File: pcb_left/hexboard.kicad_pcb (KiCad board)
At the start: 2 copper layers, 121.4 x 97.6 mm, 39 parts, among them J1 Conn_01x02_Pin, SW1 SW_Push_45deg, SW10 SW_Push_45deg, SW11 SW_Push_45deg, SW12 SW_Push_45deg, SW13 SW_Push_45deg, SW14 SW_Push_45deg, SW15 SW_Push_45deg, SW16 SW_Push_45deg, SW17 SW_Push_45deg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

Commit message: Committing any uncommitted changes
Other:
- board size 121.4 x 97.6 mm -> 209 x 97.6 mm
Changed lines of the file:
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@@
-	)
-	(gr_line
-		(start 165.590197 103.793303)
-		(end 146.590197 103.793303)
-		(stroke
-			(width 0.05)
-			(type default)
-		)
-		(layer "Edge.Cuts")
-	)
-	(gr_line
-		(start 146.090197 103.293303)
-		(end 146.090197 71.793303)
-		(stroke
-			(width 0.05)
-			(type default)
-		)
-		(layer "Edge.Cuts")
 	)
 	(gr_line
@@
 		(start 67.503125 38.1625)
 		(end 84.171875 38.1625)
+		(stroke
+			(width 0.05)
+			(type default)
+		)
+		(layer "Edge.Cuts")
+	)
+	(gr_arc
+		(start 256.2625 112.925)
+		(mid 255.969607 113.632107)
+		(end 255.2625 113.925)
 		(stroke
 			(width 0.05)
@@
 		(layer "Edge.Cuts")
 	)
-	(gr_arc
-		(start 165.590197 71.293303)
-		(mid 165.943718 71.439767)
-		(end 166.090197 71.793303)
-		(stroke
-			(width 0.05)
-			(type default)
-		)
-		(layer "Edge.Cuts")
-	)
 	(gr_line
 		(start 105.603125 38.1625)
@@
 		(layer "Edge.Cuts")
 	)
-	(gr_line
-		(start 166.090197 71.793303)
-		(end 166.090197 103.293303)
+	(gr_arc
+		(start 235.2625 113.925)
+		(mid 234.555393 113.632107)
+		(end 234.2625 112.925)
 		(stroke
 			(width 0.05)
@@
 		(layer "Edge.Cuts")
 	)
-	(gr_arc
-		(start 146.090197 71.793303)
-		(mid 146.236641 71.439732)
-		(end 146.590197 71.293303)
-		(stroke
-			(width 0.05)
-			(type default)
-		)
-		(layer "Edge.Cuts")
-	)
 	(gr_line
 		(start 86.553125 35.78125)
@@
 		(layer "Edge.Cuts")
 	)
-	(gr_arc
-		(start 146.590197 103.793303)
-		(mid 146.236676 103.646839)
-		(end 146.090197 103.293303)
+	(gr_line
+		(start 255.2625 81.925)
+		(end 235.2625 81.925)
 		(stroke
 			(width 0.05)
@@
 		(layer "Edge.Cuts")
 	)
-	(gr_arc
-		(start 166.090197 103.293303)
-		(mid 165.943753 103.646874)
-		(end 165.590197 103.793303)
+	(gr_line
+		(start 256.2625 112.925)
+		(end 256.2625 82.925)
 		(stroke
 			(width 0.05)
@@
 		(layer "Edge.Cuts")
 	)
+	(gr_line
+		(start 235.2625 113.925)
+		(end 255.2625 113.925)
+		(stroke
+			(width 0.05)
+			(type default)
+		)
+		(layer "Edge.Cuts")
+	)
 	(gr_arc
 		(start 66.3125 39.353125)
@@
 	)
 	(gr_arc
+		(start 255.2625 81.925)
+		(mid 255.969607 82.217893)
+		(end 256.2625 82.925)
+		(stroke
+			(width 0.05)
+			(type default)
+		)
+		(layer "Edge.Cuts")
+	)
+	(gr_arc
 		(start 85.3625 36.971875)
 		(mid 85.711233 36.129983)
@@
 		(layer "Edge.Cuts")
 	)
+	(gr_arc
+		(start 234.2625 82.925)
+		(mid 234.555393 82.217893)
+		(end 235.2625 81.925)
+		(stroke
+			(width 0.05)
+			(type default)
+		)
+		(layer "Edge.Cuts")
+	)
 	(gr_line
 		(start 93.696875 122.696875)
 		(end 85.3625 100.075)
-		(stroke
-			(width 0.05)
-			(type default)
-		)
-		(layer "Edge.Cuts")
-	)
-	(gr_line
-		(start 146.590197 71.293303)
-		(end 165.590197 71.293303)
 		(stroke
 			(width 0.05)
@@
 		(start 152.0375 133.4125)
 		(end 132.9875 126.26875)
+		(stroke
+			(width 0.05)
+			(type default)
+		)
+		(layer "Edge.Cuts")
+	)
+	(gr_line
+		(start 234.2625 82.925)
+		(end 234.2625 112.925)
 		(stroke
 			(width 0.05)
@@
 		)
 	)
-	(group ""
-		(members "038aaf56-ff1c-4074-8000-df0718c7a4ec" "0e31a366-141b-4baf-99b6-0dca1101d026"
-			"40619495-6268-4496-b2b6-aa191c0de21f" "506f3372-851e-4a31-bfa3-b7644925351c"
-			"635464b2-ef81-4934-a91e-93d34530852f" "79b33994-54df-4e0b-a44d-c605a84cba06"
-			"7f5ebb2b-8fa1-485b-92b2-fea6a831ab9d" "b6ac122d-b97c-4c0c-a1d2-f78f0358de96"
-		)
-	)

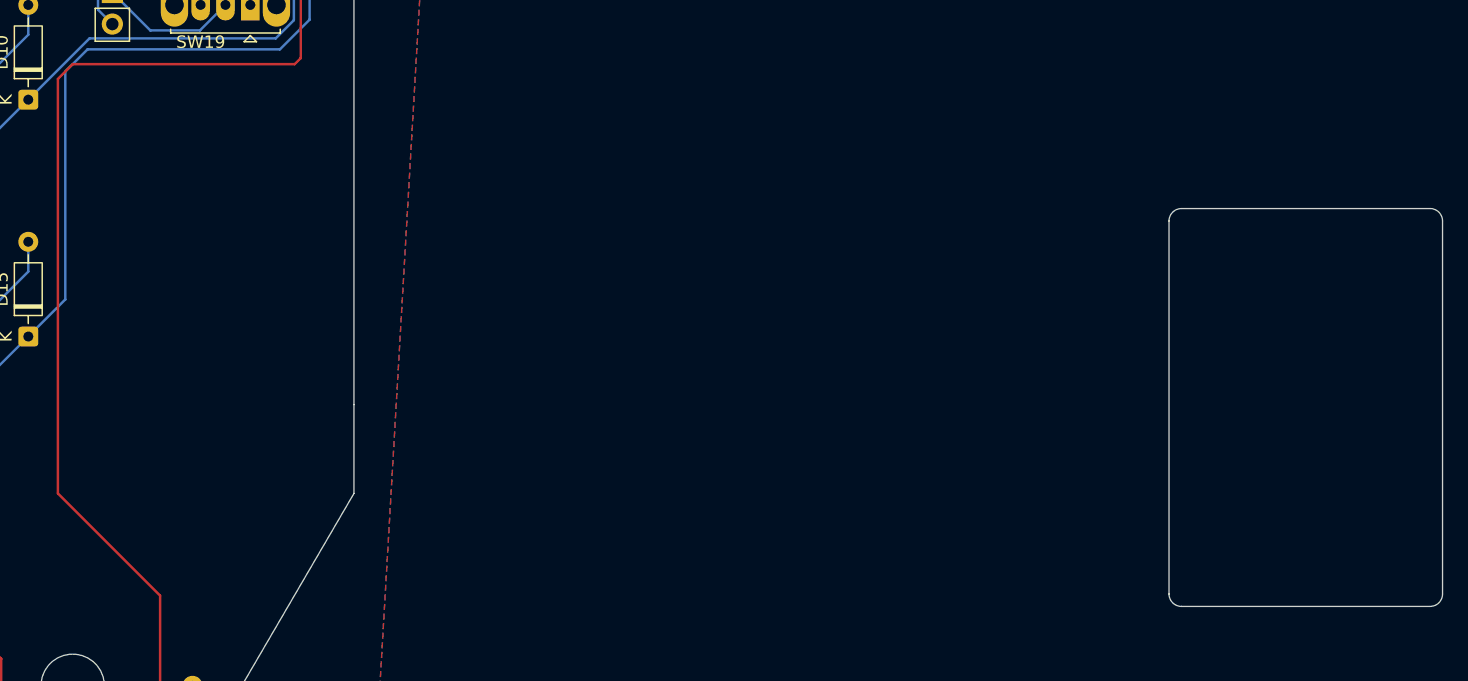
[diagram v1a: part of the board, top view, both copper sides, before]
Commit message: added design to case, colorized 3mf files
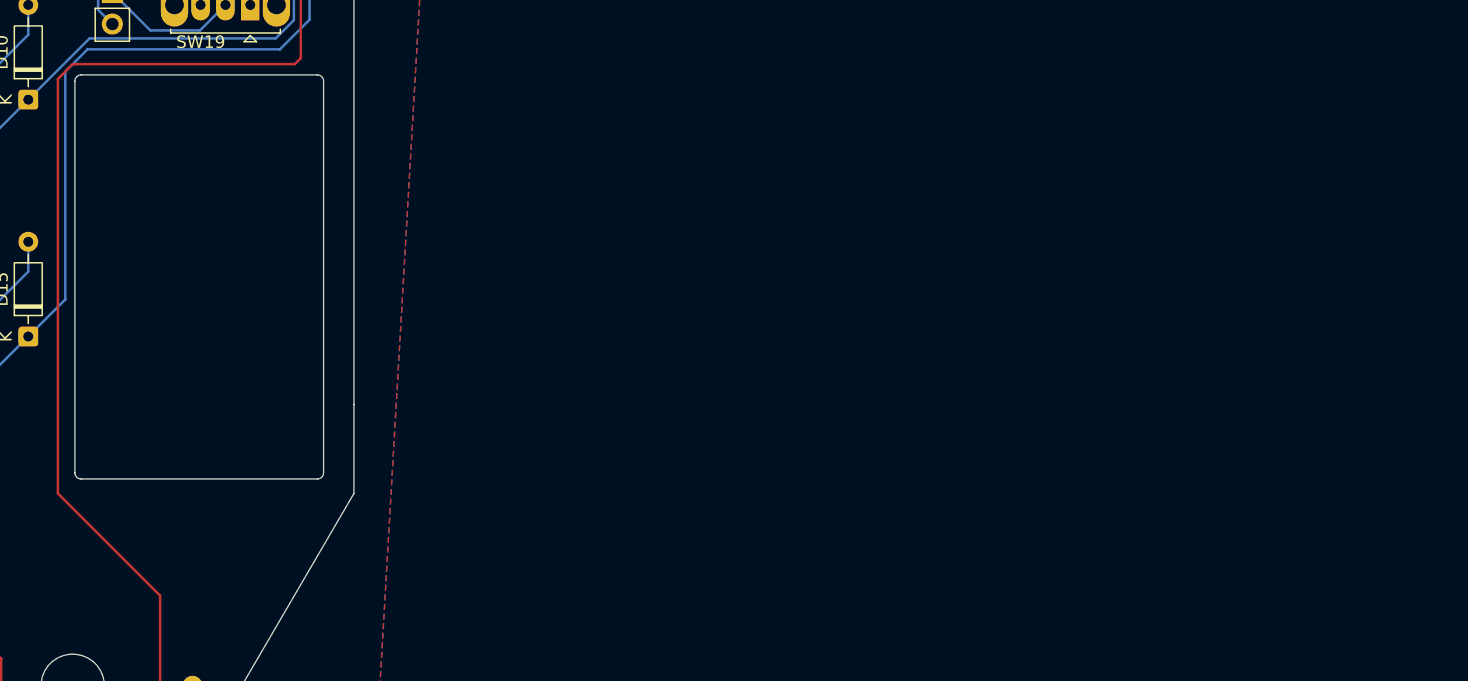
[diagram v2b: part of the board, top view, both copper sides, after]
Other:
- board size 209 x 97.6 mm -> 121.4 x 97.6 mm
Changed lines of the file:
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@@
 		(embedded_fonts no)
+	)
+	(gr_arc
+		(start 166.2625 103.175)
+		(mid 166.116023 103.528523)
+		(end 165.7625 103.675)
+		(stroke
+			(width 0.05)
+			(type default)
+		)
+		(layer "Edge.Cuts")
+	)
+	(gr_line
+		(start 146.7625 103.675)
+		(end 165.7625 103.675)
+		(stroke
+			(width 0.05)
+			(type default)
+		)
+		(layer "Edge.Cuts")
 	)
 	(gr_line
@@
 		(start 67.503125 38.1625)
 		(end 84.171875 38.1625)
-		(stroke
-			(width 0.05)
-			(type default)
-		)
-		(layer "Edge.Cuts")
-	)
-	(gr_arc
-		(start 256.2625 112.925)
-		(mid 255.969607 113.632107)
-		(end 255.2625 113.925)
 		(stroke
 			(width 0.05)
@@
 		(layer "Edge.Cuts")
 	)
+	(gr_line
+		(start 166.2625 103.175)
+		(end 166.2625 71.675)
+		(stroke
+			(width 0.05)
+			(type default)
+		)
+		(layer "Edge.Cuts")
+	)
 	(gr_arc
 		(start 105.603125 38.1625)
@@
 		(layer "Edge.Cuts")
 	)
-	(gr_arc
-		(start 235.2625 113.925)
-		(mid 234.555393 113.632107)
-		(end 234.2625 112.925)
+	(gr_line
+		(start 165.7625 71.175)
+		(end 146.7625 71.175)
 		(stroke
 			(width 0.05)
@@
 	)
 	(gr_line
-		(start 255.2625 81.925)
-		(end 235.2625 81.925)
-		(stroke
-			(width 0.05)
-			(type default)
-		)
-		(layer "Edge.Cuts")
-	)
-	(gr_line
 		(start 66.3125 41.734375)
 		(end 66.3125 39.353125)
@@
 		(layer "Edge.Cuts")
 	)
-	(gr_line
-		(start 256.2625 112.925)
-		(end 256.2625 82.925)
+	(gr_arc
+		(start 165.7625 71.175)
+		(mid 166.11605 71.321448)
+		(end 166.2625 71.675)
 		(stroke
 			(width 0.05)
@@
 		(layer "Edge.Cuts")
 	)
-	(gr_line
-		(start 235.2625 113.925)
-		(end 255.2625 113.925)
+	(gr_arc
+		(start 146.2625 71.675)
+		(mid 146.408975 71.321475)
+		(end 146.7625 71.175)
 		(stroke
 			(width 0.05)
@@
 	)
 	(gr_arc
-		(start 255.2625 81.925)
-		(mid 255.969607 82.217893)
-		(end 256.2625 82.925)
-		(stroke
-			(width 0.05)
-			(type default)
-		)
-		(layer "Edge.Cuts")
-	)
-	(gr_arc
 		(start 85.3625 36.971875)
 		(mid 85.711233 36.129983)
@@
 		(layer "Edge.Cuts")
 	)
-	(gr_arc
-		(start 234.2625 82.925)
-		(mid 234.555393 82.217893)
-		(end 235.2625 81.925)
-		(stroke
-			(width 0.05)
-			(type default)
-		)
-		(layer "Edge.Cuts")
-	)
 	(gr_line
 		(start 93.696875 122.696875)
 		(end 85.3625 100.075)
+		(stroke
+			(width 0.05)
+			(type default)
+		)
+		(layer "Edge.Cuts")
+	)
+	(gr_arc
+		(start 146.7625 103.675)
+		(mid 146.408944 103.528555)
+		(end 146.2625 103.175)
+		(stroke
+			(width 0.05)
+			(type default)
+		)
+		(layer "Edge.Cuts")
+	)
+	(gr_line
+		(start 146.2625 71.675)
+		(end 146.2625 103.175)
 		(stroke
 			(width 0.05)
@@
 		(start 152.0375 133.4125)
 		(end 132.9875 126.26875)
-		(stroke
-			(width 0.05)
-			(type default)
-		)
-		(layer "Edge.Cuts")
-	)
-	(gr_line
-		(start 234.2625 82.925)
-		(end 234.2625 112.925)
 		(stroke
 			(width 0.05)
@@
 		)
 	)
+	(group ""
+		(members "00e43715-53f3-4ea1-98fc-cb59ef5a5fb9" "155b0c59-fafb-4c57-ae90-0c5d199b792e"
+			"496fec20-f23c-4671-a5c3-d85c3c0f6db6" "505f9bb3-b023-4d03-9e19-543c4c57f35f"
+			"81639af1-5ace-4db3-aaf6-bfacb273b448" "919c6895-5915-4b07-a29b-89a69136c541"
+			"d376d5af-8dc7-481c-86ed-2687451803a4" "e376f95c-ef53-4611-9724-5e1a350fe638"
+		)
+	)
